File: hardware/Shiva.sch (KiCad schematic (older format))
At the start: 101 parts, among them J1 JACK_FEMALE_STEREO, J2 JACK_FEMALE_STEREO, J3 JACK_FEMALE_STEREO, J4 JACK_FEMALE_STEREO, J5 JACK_FEMALE_STEREO, J6 JACK_FEMALE_STEREO, J7 JACK_FEMALE_STEREO, J8 JACK_FEMALE_STEREO, P1 DIN_5, Q1 2N7002, Q2 2N7002, Q3 2N7002, Q4 2N7002, Q5 2N7002, Q6 2N7002, Q7 2N7002, Q8 2N7002, U1 LTC6242, U2 LTC6242, U3 LD1117S33CTR

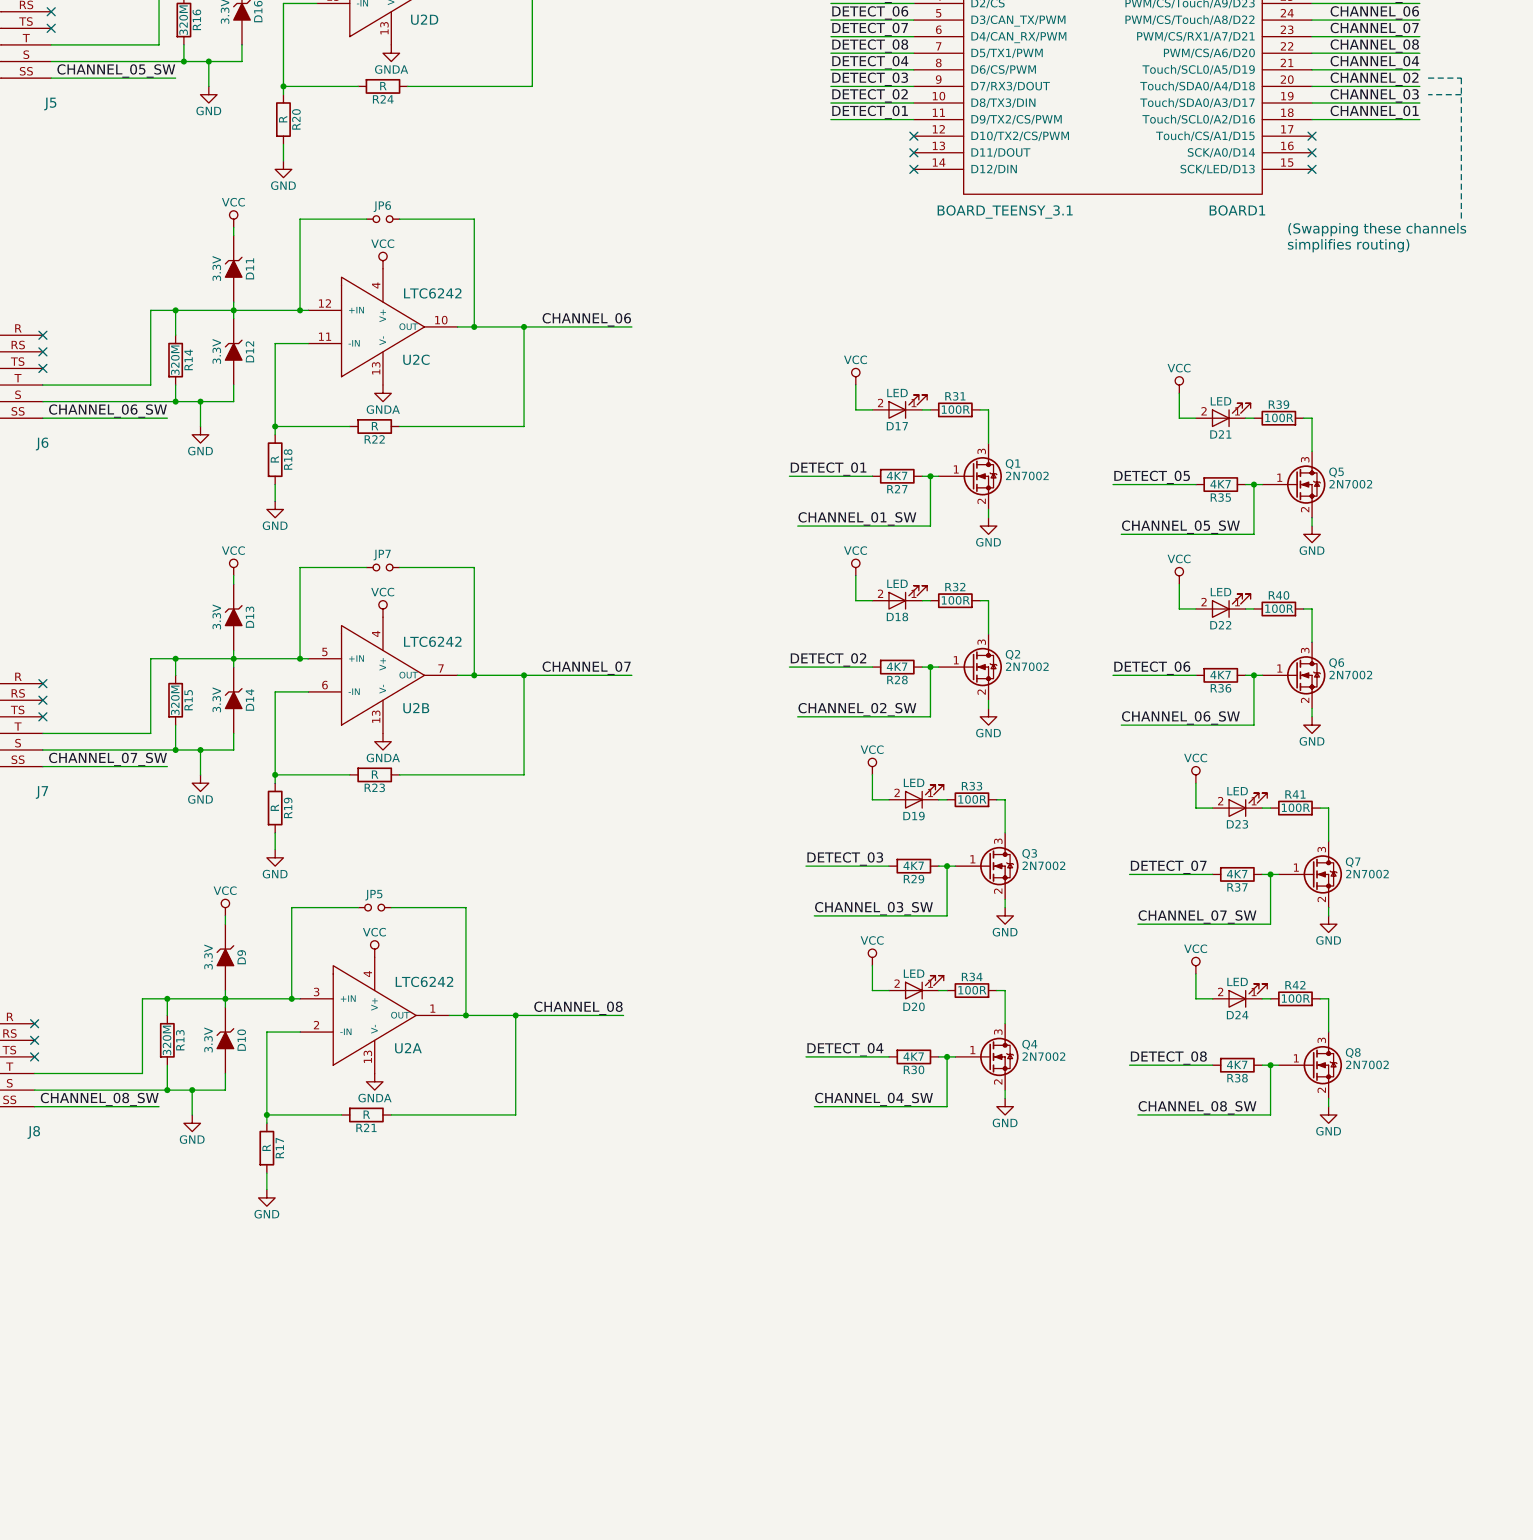
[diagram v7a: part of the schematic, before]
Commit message: Add 5-way joystick as user interface
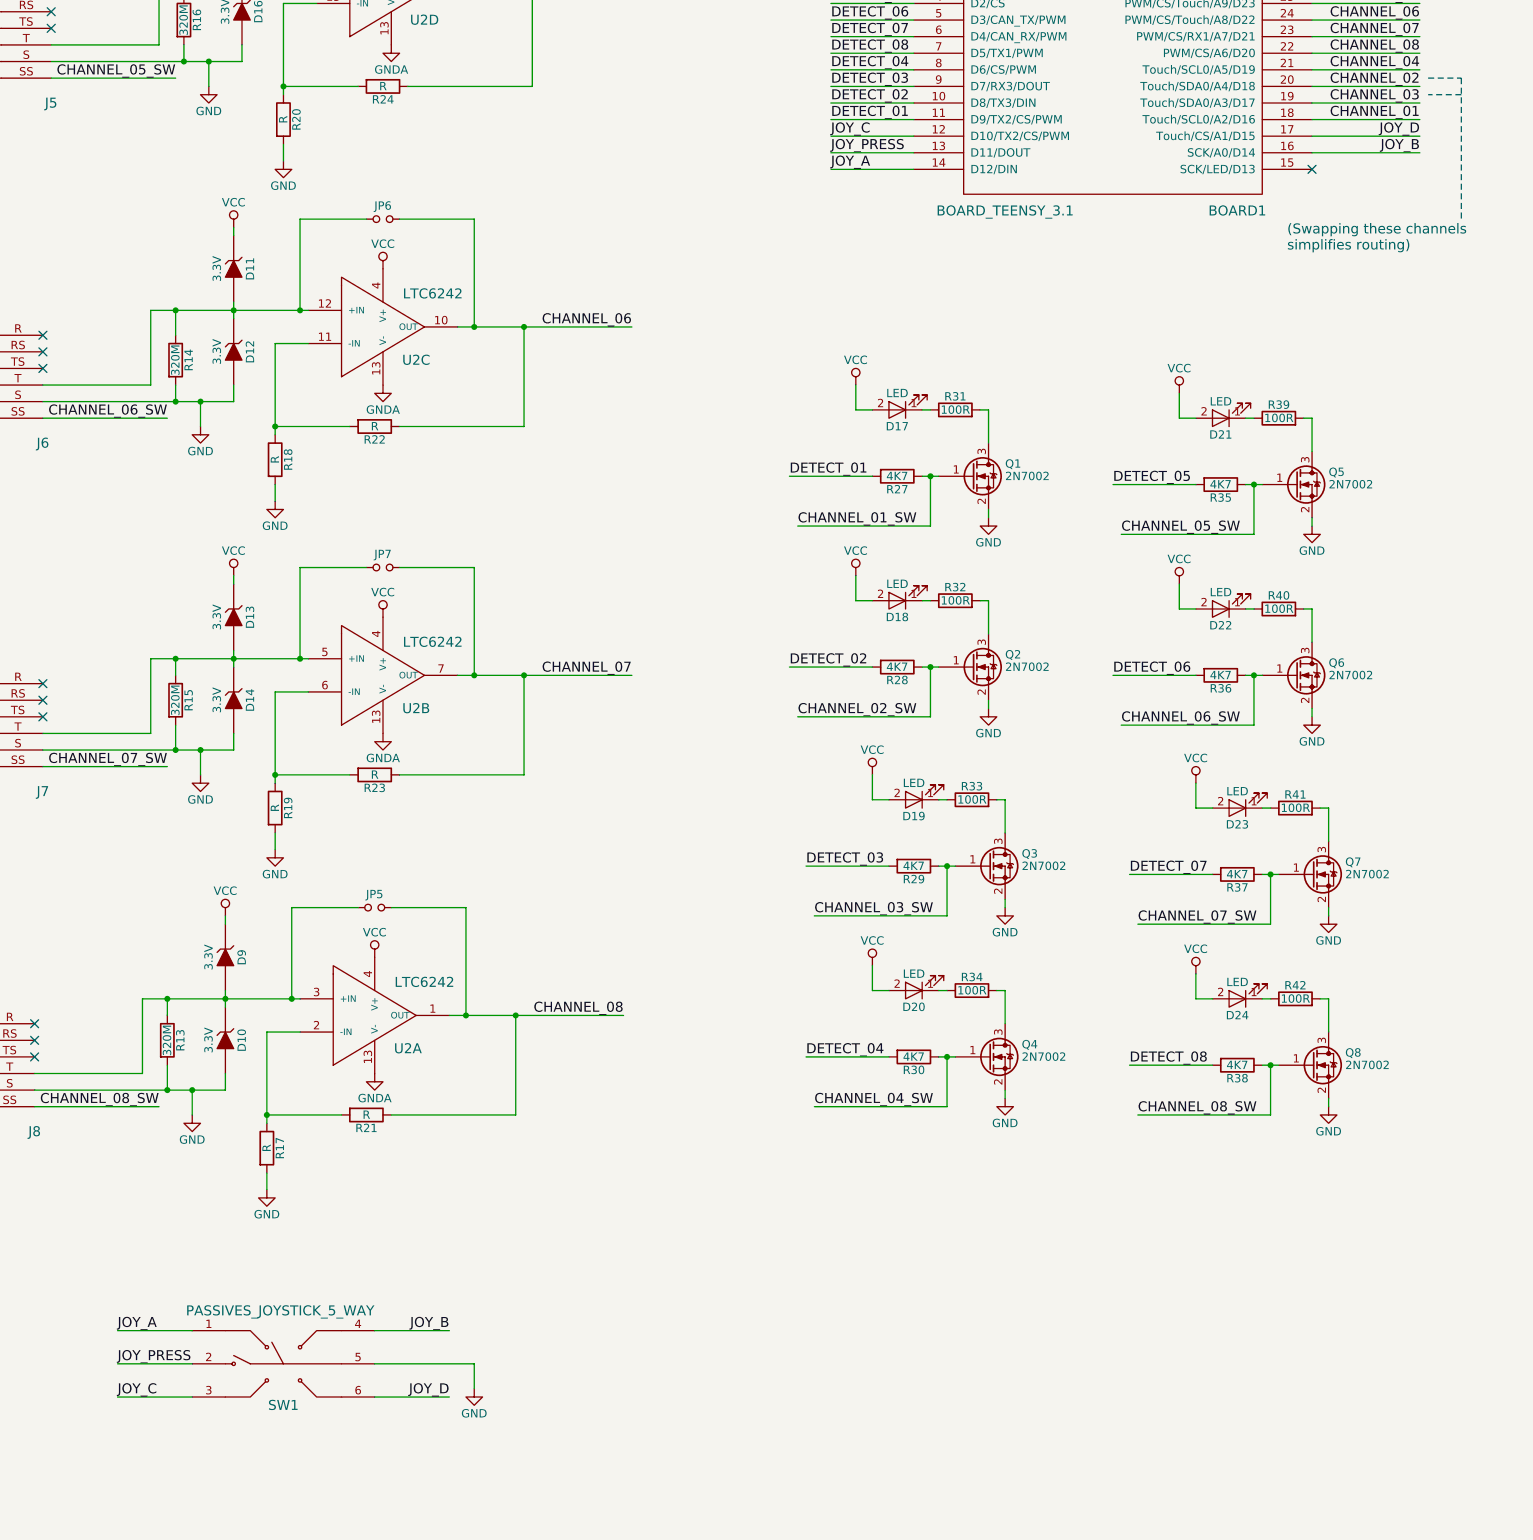
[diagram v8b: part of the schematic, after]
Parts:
- added SW1: PASSIVES_JOYSTICK_5_WAY, def-footprints:Switches_ALPS-SKRHAAE010, symbol PASSIVES_JOYSTICK_5_WAY
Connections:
- net GND: now also SW1.5
- net JOY_C: now reaches BOARD1.12 (D10/TX2/CS/PWM)
- net JOY_C: now also SW1.3
- net JOY_PRESS: now reaches BOARD1.13 (D11/DOUT)
- net JOY_PRESS: now also SW1.2
- net JOY_A: now reaches BOARD1.14 (D12/DIN)
- net JOY_A: now also SW1.1
- net JOY_B: now reaches BOARD1.16 (SCK/A0/D14)
- net JOY_B: now also SW1.4
- net JOY_D: now reaches BOARD1.17 (Touch/CS/A1/D15)
- net JOY_D: now also SW1.6
- no-connect marks 34 -> 29
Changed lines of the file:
@@
 Wire Wire Line
 	11900 1450 12550 1450
-NoConn ~ 12550 2550
-NoConn ~ 12550 2650
-NoConn ~ 12550 2750
 NoConn ~ 14950 2750
-NoConn ~ 14950 2650
-NoConn ~ 14950 2550
 $Comp
 L GNDA #PWR045
@@
 	1    0    0    -1
 $EndComp
+$Comp
+L PASSIVES_JOYSTICK_5_WAY SW1
+U 1 1 5AB6FB60
+P 8750 9950
+F 0 "SW1" H 8750 9700 60  0000 C CNN
+F 1 "PASSIVES_JOYSTICK_5_WAY" H 8730 10270 60  0000 C CNN
+F 2 "def-footprints:Switches_ALPS-SKRHAAE010" H 8750 9950 60  0001 C CNN
+F 3 "" H 8750 9950 60  0001 C CNN
+	1    8750 9950
+	1    0    0    -1
+$EndComp
+$Comp
+L GND #PWR078
+U 1 1 5AB6FFA3
+P 9900 10100
+F 0 "#PWR078" H 9900 9850 50  0001 C CNN
+F 1 "GND" H 9900 9950 50  0000 C CNN
+F 2 "" H 9900 10100 60  0000 C CNN
+F 3 "" H 9900 10100 60  0000 C CNN
+	1    9900 10100
+	1    0    0    -1
+$EndComp
+Wire Wire Line
+	9900 10100 9900 9950
+Wire Wire Line
+	9900 9950 9300 9950
+Wire Wire Line
+	8200 9750 7750 9750
+Text Label 7750 9750 0    60   ~ 0
+JOY_A
+Wire Wire Line
+	8200 10150 7750 10150
+Text Label 7750 10150 0    60   ~ 0
+JOY_C
+Wire Wire Line
+	9300 9750 9750 9750
+Text Label 9750 9750 2    60   ~ 0
+JOY_B
+Wire Wire Line
+	9300 10150 9750 10150
+Text Label 9750 10150 2    60   ~ 0
+JOY_D
+Wire Wire Line
+	8200 9950 7750 9950
+Text Label 7750 9950 0    60   ~ 0
+JOY_PRESS
+Wire Wire Line
+	12050 2550 12550 2550
+Text Label 12050 2750 0    60   ~ 0
+JOY_A
+Wire Wire Line
+	12050 2650 12550 2650
+Text Label 12050 2550 0    60   ~ 0
+JOY_C
+Wire Wire Line
+	12050 2750 12550 2750
+Text Label 12050 2650 0    60   ~ 0
+JOY_PRESS
+Wire Wire Line
+	14950 2550 15600 2550
+Text Label 15600 2650 2    60   ~ 0
+JOY_B
+Wire Wire Line
+	14950 2650 15600 2650
+Text Label 15600 2550 2    60   ~ 0
+JOY_D
 $EndSCHEMATC
